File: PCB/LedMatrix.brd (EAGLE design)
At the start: 32.3 x 33.7 mm, 12 parts, among them IC1 74HC164D

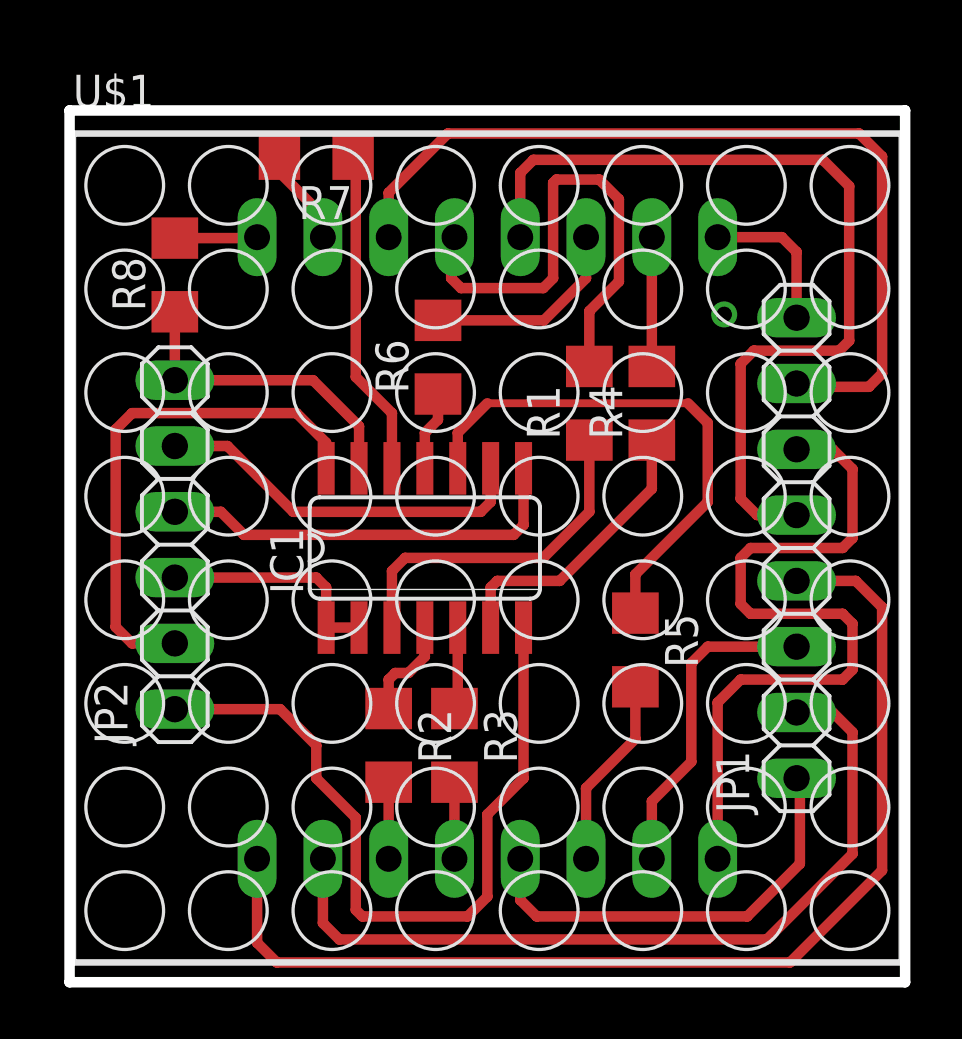
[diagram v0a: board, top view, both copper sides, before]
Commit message: Updated led matrix board.
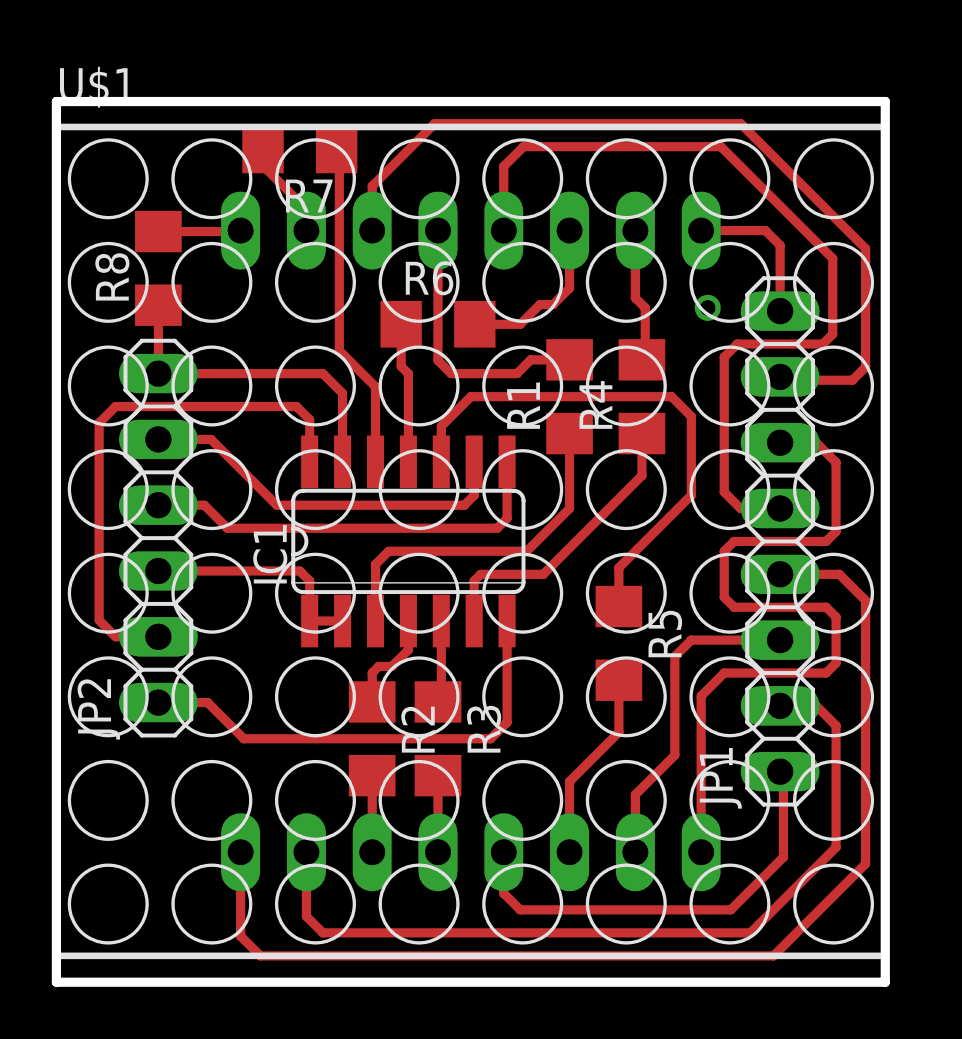
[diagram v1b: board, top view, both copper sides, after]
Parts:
- moved R6 1.27 mm to (14.7, 25.4), turned to 0 degrees
- moved R1 0.80 mm to (19.8, 22.6)
- moved U$1 0.68 mm to (16.0, 17.0)
- moved R3 0.68 mm to (14.7, 9.40)
- moved R5 0.68 mm to (21.7, 13.1)
- moved JP2 0.68 mm to (3.94, 17.1)
- moved R8 0.68 mm to (3.94, 27.6)
- moved IC1 0.68 mm to (13.6, 17.0)
- moved R7 0.68 mm to (9.40, 32.1)
- moved R2 0.68 mm to (12.2, 9.40)
- moved JP1 0.68 mm to (27.9, 17.0)
- moved R4 0.46 mm to (22.6, 22.6)
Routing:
- net GND: track 29.5 -> 18.2 mm
- net N$1: track 19.4 -> 10.5 mm
- net N$14: track 3.08 -> 5.42 mm
- net N$18: track 34.0 -> 31.9 mm
- net N$20: track 34.0 -> 32.4 mm
- net N$6: track 7.97 -> 6.46 mm
- net N$16: track 12.1 -> 12.7 mm
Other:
- board size 32.3 x 33.7 mm -> 32 x 34 mm

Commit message: Minor corrections to the led matrix board.
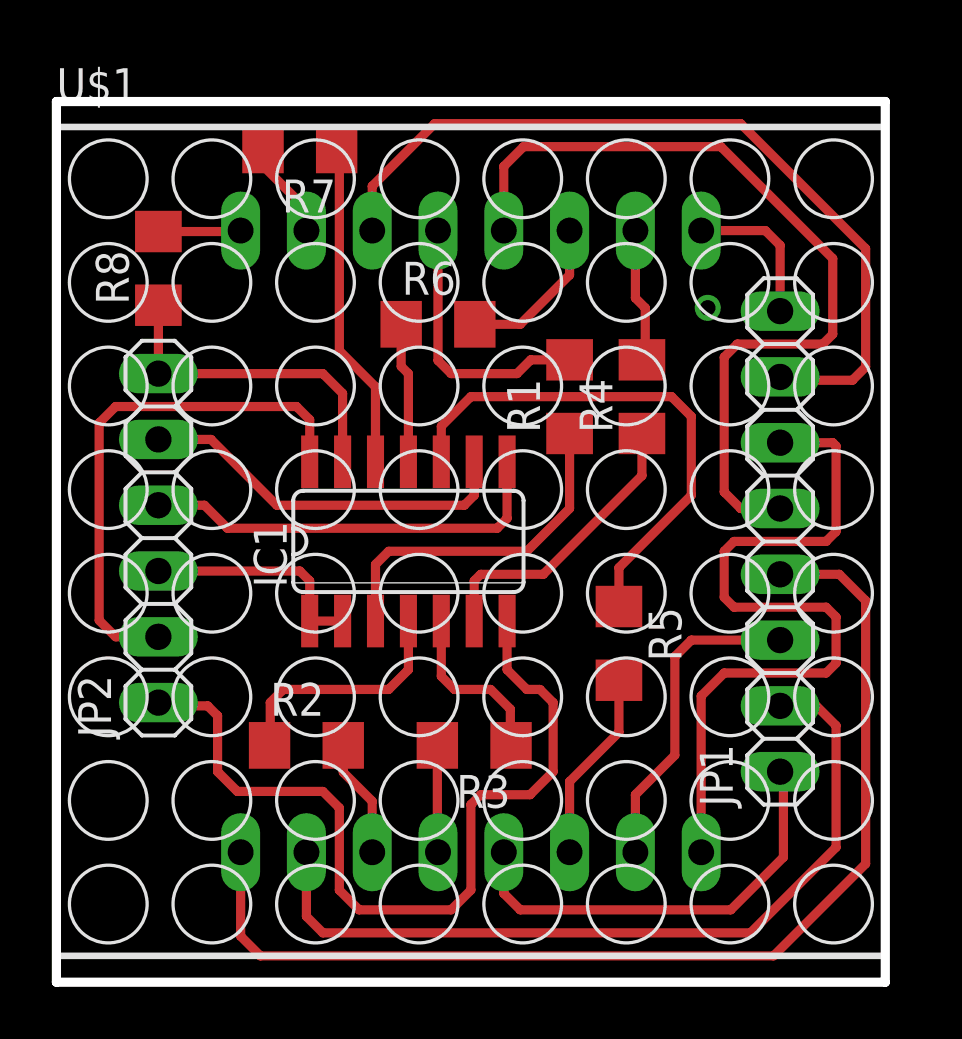
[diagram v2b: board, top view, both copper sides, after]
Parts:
- moved R2 2.55 mm to (9.65, 9.14), turned to 0 degrees
- moved R3 1.42 mm to (16.1, 9.14), turned to 180 degrees
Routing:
- net GND: track 18.2 -> 32.7 mm
- net N$10: track 4.00 -> 9.40 mm
- net N$11: track 3.18 -> 6.73 mm
- net N$2: track 2.96 -> 4.59 mm
- net N$3: track 2.96 -> 4.14 mm
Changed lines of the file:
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@@
 <setting verticaltext="up"/>
 </settings>
-<grid distance="1" unitdist="mm" unit="mm" style="lines" multiple="1" display="yes" altdistance="5" altunitdist="mil" altunit="mil"/>
+<grid distance="5" unitdist="mil" unit="mil" style="lines" multiple="1" display="yes" altdistance="5" altunitdist="mil" altunit="mil"/>
 <layers>
 <layer number="1" name="Top" color="4" fill="1" visible="yes" active="yes"/>
@@
 <element name="R1" library="resistor" package="R1206" value="200" x="19.812" y="22.606" rot="R90"/>
 <element name="U$1" library="led_matrix_8x8" package="NFM-12881BG-11" value="NFM-12881BG-11" x="16.002" y="17.018"/>
-<element name="R2" library="resistor" package="R1206" value="200" x="12.192" y="9.398" rot="R270"/>
-<element name="R3" library="resistor" package="R1206" value="200" x="14.732" y="9.398" rot="R270"/>
+<element name="R2" library="resistor" package="R1206" value="200" x="9.652" y="9.144"/>
+<element name="R3" library="resistor" package="R1206" value="200" x="16.129" y="9.144" rot="R180"/>
 <element name="R4" library="resistor" package="R1206" value="200" x="22.606" y="22.606" rot="R90"/>
 <element name="R5" library="resistor" package="R1206" value="200" x="21.717" y="13.081" rot="R270"/>
@@
 <contactref element="IC1" pad="7"/>
 <contactref element="JP2" pad="1"/>
-<wire x1="17.399" y1="13.9446" x2="17.399" y2="10.033" width="0.3556" layer="1"/>
-<wire x1="17.399" y1="10.033" x2="16.764" y2="9.398" width="0.3556" layer="1"/>
-<wire x1="16.764" y1="9.398" x2="7.239" y2="9.398" width="0.3556" layer="1"/>
-<wire x1="7.239" y1="9.398" x2="5.842" y2="10.795" width="0.3556" layer="1"/>
-<wire x1="5.842" y1="10.795" x2="3.937" y2="10.795" width="0.3556" layer="1"/>
+<wire x1="17.399" y1="13.9446" x2="17.399" y2="12.065" width="0.3556" layer="1"/>
+<wire x1="17.399" y1="12.065" x2="18.161" y2="11.303" width="0.3556" layer="1"/>
+<wire x1="18.161" y1="11.303" x2="18.669" y2="11.303" width="0.3556" layer="1"/>
+<wire x1="18.669" y1="11.303" x2="19.177" y2="10.795" width="0.3556" layer="1"/>
+<wire x1="19.177" y1="10.795" x2="19.177" y2="8.128" width="0.3556" layer="1"/>
+<wire x1="19.177" y1="8.128" x2="18.288" y2="7.239" width="0.3556" layer="1"/>
+<wire x1="18.288" y1="7.239" x2="16.383" y2="7.239" width="0.3556" layer="1"/>
+<wire x1="16.383" y1="7.239" x2="16.002" y2="6.858" width="0.3556" layer="1"/>
+<wire x1="16.002" y1="6.858" x2="16.002" y2="3.556" width="0.3556" layer="1"/>
+<wire x1="16.002" y1="3.556" x2="15.24" y2="2.794" width="0.3556" layer="1"/>
+<wire x1="15.24" y1="2.794" x2="11.684" y2="2.794" width="0.3556" layer="1"/>
+<wire x1="11.684" y1="2.794" x2="10.922" y2="3.556" width="0.3556" layer="1"/>
+<wire x1="10.922" y1="3.556" x2="10.922" y2="6.731" width="0.3556" layer="1"/>
+<wire x1="10.922" y1="6.731" x2="10.287" y2="7.366" width="0.3556" layer="1"/>
+<wire x1="10.287" y1="7.366" x2="6.985" y2="7.366" width="0.3556" layer="1"/>
+<wire x1="6.985" y1="7.366" x2="6.223" y2="8.128" width="0.3556" layer="1"/>
+<wire x1="6.223" y1="8.128" x2="6.223" y2="10.287" width="0.3556" layer="1"/>
+<wire x1="6.223" y1="10.287" x2="5.842" y2="10.668" width="0.3556" layer="1"/>
+<wire x1="5.842" y1="10.668" x2="4.064" y2="10.668" width="0.3556" layer="1"/>
+<wire x1="4.064" y1="10.668" x2="3.937" y2="10.795" width="0.3556" layer="1"/>
 </signal>
 <signal name="VCC">
@@
 <contactref element="U$1" pad="3"/>
 <contactref element="R2" pad="2"/>
-<wire x1="12.192" y1="7.976" x2="12.192" y2="5.018" width="0.3556" layer="1"/>
+<wire x1="11.074" y1="9.144" x2="11.074" y2="8.103" width="0.3556" layer="1"/>
+<wire x1="11.074" y1="8.103" x2="12.192" y2="6.985" width="0.3556" layer="1"/>
+<wire x1="12.192" y1="6.985" x2="12.192" y2="5.018" width="0.3556" layer="1"/>
 </signal>
 <signal name="N$3">
 <contactref element="U$1" pad="4"/>
 <contactref element="R3" pad="2"/>
-<wire x1="14.732" y1="7.976" x2="14.732" y2="5.018" width="0.3556" layer="1"/>
+<wire x1="14.707" y1="9.144" x2="14.707" y2="5.043" width="0.3556" layer="1"/>
+<wire x1="14.707" y1="5.043" x2="14.732" y2="5.018" width="0.3556" layer="1"/>
 </signal>
 <signal name="N$4">
@@
 <contactref element="U$1" pad="11"/>
 <contactref element="R6" pad="2"/>
-<wire x1="19.812" y1="29.018" x2="19.812" y2="26.797" width="0.3556" layer="1"/>
-<wire x1="19.812" y1="26.797" x2="19.177" y2="26.162" width="0.3556" layer="1"/>
-<wire x1="19.177" y1="26.162" x2="18.669" y2="26.162" width="0.3556" layer="1"/>
-<wire x1="18.669" y1="26.162" x2="17.907" y2="25.4" width="0.3556" layer="1"/>
+<wire x1="19.812" y1="29.018" x2="19.812" y2="27.305" width="0.3556" layer="1"/>
+<wire x1="19.812" y1="27.305" x2="17.907" y2="25.4" width="0.3556" layer="1"/>
 <wire x1="17.907" y1="25.4" x2="16.154" y2="25.4" width="0.3556" layer="1"/>
 </signal>
@@
 <contactref element="R2" pad="1"/>
 <contactref element="IC1" pad="4"/>
-<wire x1="13.589" y1="13.9446" x2="13.589" y2="12.827" width="0.3556" layer="1"/>
-<wire x1="13.589" y1="12.827" x2="12.954" y2="12.192" width="0.3556" layer="1"/>
-<wire x1="12.954" y1="12.192" x2="12.446" y2="12.192" width="0.3556" layer="1"/>
-<wire x1="12.446" y1="12.192" x2="12.192" y2="11.938" width="0.3556" layer="1"/>
-<wire x1="12.192" y1="11.938" x2="12.192" y2="10.82" width="0.3556" layer="1"/>
+<wire x1="13.589" y1="13.9446" x2="13.589" y2="12.065" width="0.3556" layer="1"/>
+<wire x1="13.589" y1="12.065" x2="12.827" y2="11.303" width="0.3556" layer="1"/>
+<wire x1="12.827" y1="11.303" x2="8.763" y2="11.303" width="0.3556" layer="1"/>
+<wire x1="8.763" y1="11.303" x2="8.255" y2="10.795" width="0.3556" layer="1"/>
+<wire x1="8.255" y1="10.795" x2="8.255" y2="9.169" width="0.3556" layer="1"/>
+<wire x1="8.255" y1="9.169" x2="8.23" y2="9.144" width="0.3556" layer="1"/>
 </signal>
 <signal name="N$11">
 <contactref element="R3" pad="1"/>
 <contactref element="IC1" pad="5"/>
-<wire x1="14.859" y1="13.9446" x2="14.859" y2="10.947" width="0.3556" layer="1"/>
-<wire x1="14.859" y1="10.947" x2="14.732" y2="10.82" width="0.3556" layer="1"/>
+<wire x1="14.859" y1="13.9446" x2="14.859" y2="11.811" width="0.3556" layer="1"/>
+<wire x1="14.859" y1="11.811" x2="15.367" y2="11.303" width="0.3556" layer="1"/>
+<wire x1="15.367" y1="11.303" x2="16.764" y2="11.303" width="0.3556" layer="1"/>
+<wire x1="16.764" y1="11.303" x2="17.526" y2="10.541" width="0.3556" layer="1"/>
+<wire x1="17.526" y1="10.541" x2="17.526" y2="9.169" width="0.3556" layer="1"/>
+<wire x1="17.526" y1="9.169" x2="17.551" y2="9.144" width="0.3556" layer="1"/>
 </signal>
 <signal name="N$12">
@@
 <wire x1="26.162" y1="17.018" x2="29.718" y2="17.018" width="0.3556" layer="1"/>
 <wire x1="29.718" y1="17.018" x2="30.099" y2="17.399" width="0.3556" layer="1"/>
-<wire x1="30.099" y1="17.399" x2="30.099" y2="20.066" width="0.3556" layer="1"/>
-<wire x1="30.099" y1="20.066" x2="29.337" y2="20.828" width="0.3556" layer="1"/>
-<wire x1="29.337" y1="20.828" x2="27.94" y2="20.828" width="0.3556" layer="1"/>
+<wire x1="30.099" y1="17.399" x2="30.099" y2="20.701" width="0.3556" layer="1"/>
+<wire x1="29.972" y1="20.828" x2="27.94" y2="20.828" width="0.3556" layer="1"/>
+<wire x1="29.972" y1="20.828" x2="30.099" y2="20.701" width="0.3556" layer="1"/>
 </signal>
 <signal name="N$20">
@@
 <wire x1="17.399" y1="17.907" x2="17.018" y2="17.526" width="0.3556" layer="1"/>
 <contactref element="JP2" pad="4"/>
-<wire x1="6.604" y1="17.526" x2="5.715" y2="18.415" width="0.3556" layer="1"/>
 <wire x1="5.715" y1="18.415" x2="3.937" y2="18.415" width="0.3556" layer="1"/>
+<wire x1="5.715" y1="18.415" x2="6.604" y2="17.526" width="0.3556" layer="1"/>
 </signal>
 <signal name="N$25">

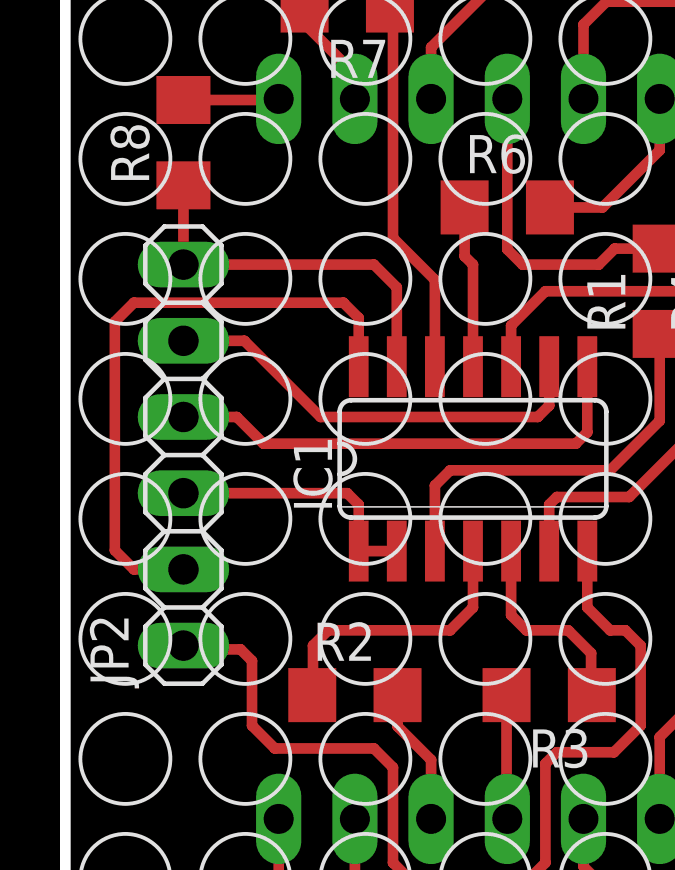
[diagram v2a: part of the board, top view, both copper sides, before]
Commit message: Minor measure corrections on the matrix board.
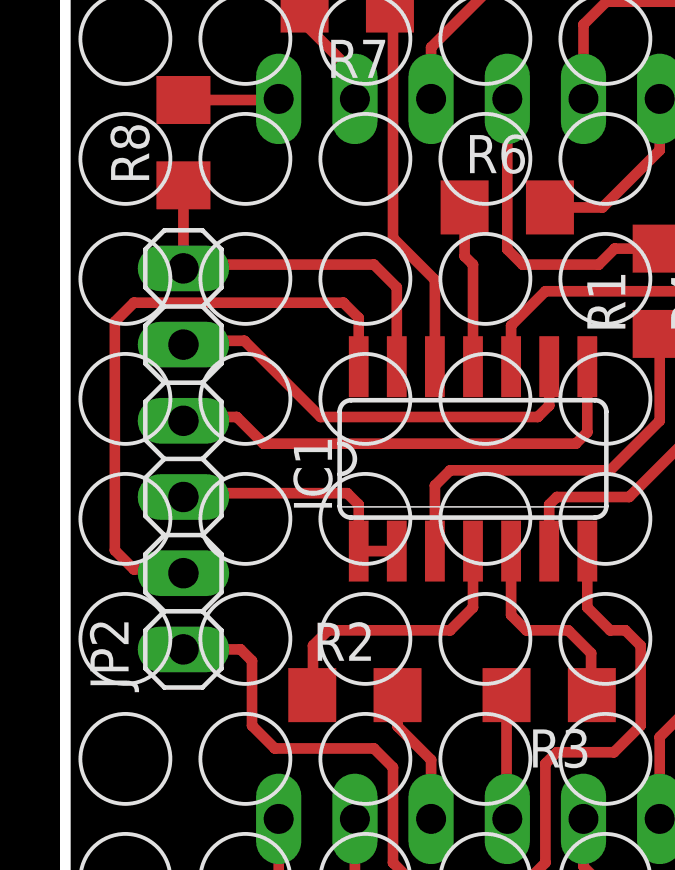
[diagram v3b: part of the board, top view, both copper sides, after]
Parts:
- moved JP2 0.13 mm to (3.94, 17.0)
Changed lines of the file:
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@@
 <dimension x1="0" y1="0" x2="4" y2="0" x3="2" y3="-3" textsize="1.016" layer="47"/>
 <dimension x1="32" y1="0" x2="28" y2="0" x3="30" y3="-3" textsize="1.016" layer="47"/>
+<dimension x1="0" y1="0" x2="0" y2="17" x3="37" y3="8.5" textsize="1.016" layer="47"/>
 </plain>
 <attributes>
@@
 <element name="R8" library="resistor" package="R1206" value="200" x="3.937" y="27.559" rot="R90"/>
 <element name="JP1" library="pinhead" package="1X08" value="" x="27.94" y="17.018" rot="R90"/>
-<element name="JP2" library="pinhead" package="1X06" value="" x="3.937" y="17.145" rot="R90"/>
+<element name="JP2" library="pinhead" package="1X06" value="" x="3.937" y="17.018" rot="R90"/>
 </elements>
 <signals>
@@
 <wire x1="6.223" y1="8.128" x2="6.223" y2="10.287" width="0.3556" layer="1"/>
 <wire x1="6.223" y1="10.287" x2="5.842" y2="10.668" width="0.3556" layer="1"/>
-<wire x1="5.842" y1="10.668" x2="4.064" y2="10.668" width="0.3556" layer="1"/>
-<wire x1="4.064" y1="10.668" x2="3.937" y2="10.795" width="0.3556" layer="1"/>
+<wire x1="3.937" y1="10.668" x2="5.842" y2="10.668" width="0.3556" layer="1"/>
 </signal>
 <signal name="VCC">
@@
 <contactref element="JP2" pad="2"/>
 <wire x1="9.271" y1="22.225" x2="2.286" y2="22.225" width="0.3556" layer="1"/>
-<wire x1="3.937" y1="13.335" x2="2.286" y2="13.335" width="0.3556" layer="1"/>
 <wire x1="2.286" y1="13.335" x2="1.651" y2="13.97" width="0.3556" layer="1"/>
 <wire x1="1.651" y1="13.97" x2="1.651" y2="21.59" width="0.3556" layer="1"/>
@@
 <wire x1="9.779" y1="20.0914" x2="9.779" y2="21.717" width="0.3556" layer="1"/>
 <wire x1="9.779" y1="21.717" x2="9.271" y2="22.225" width="0.3556" layer="1"/>
+<wire x1="2.286" y1="13.335" x2="3.81" y2="13.335" width="0.3556" layer="1"/>
+<wire x1="3.81" y1="13.335" x2="3.937" y2="13.208" width="0.3556" layer="1"/>
 </signal>
 <signal name="N$1">
@@
 <contactref element="IC1" pad="13"/>
 <contactref element="JP2" pad="6"/>
-<wire x1="10.287" y1="23.495" x2="3.937" y2="23.495" width="0.3556" layer="1"/>
-<wire x1="3.937" y1="23.495" x2="3.937" y2="26.137" width="0.3556" layer="1"/>
 <wire x1="11.049" y1="20.0914" x2="11.049" y2="22.733" width="0.3556" layer="1"/>
 <wire x1="11.049" y1="22.733" x2="10.287" y2="23.495" width="0.3556" layer="1"/>
+<wire x1="10.287" y1="23.495" x2="4.064" y2="23.495" width="0.3556" layer="1"/>
+<wire x1="4.064" y1="23.495" x2="3.937" y2="23.368" width="0.3556" layer="1"/>
+<wire x1="3.937" y1="26.137" x2="3.937" y2="23.368" width="0.3556" layer="1"/>
 </signal>
 <signal name="N$17">
@@
 <wire x1="11.049" y1="13.9446" x2="9.779" y2="13.9446" width="0.3556" layer="1"/>
 <contactref element="JP2" pad="3"/>
-<wire x1="3.937" y1="15.875" x2="9.398" y2="15.875" width="0.3556" layer="1"/>
 <wire x1="9.398" y1="15.875" x2="9.779" y2="15.494" width="0.3556" layer="1"/>
 <wire x1="9.779" y1="15.494" x2="9.779" y2="13.9446" width="0.3556" layer="1"/>
+<wire x1="9.398" y1="15.875" x2="4.064" y2="15.875" width="0.3556" layer="1"/>
+<wire x1="4.064" y1="15.875" x2="3.937" y2="15.748" width="0.3556" layer="1"/>
 </signal>
 <signal name="N$27">
@@
 <wire x1="17.399" y1="17.907" x2="17.018" y2="17.526" width="0.3556" layer="1"/>
 <contactref element="JP2" pad="4"/>
-<wire x1="5.715" y1="18.415" x2="3.937" y2="18.415" width="0.3556" layer="1"/>
 <wire x1="5.715" y1="18.415" x2="6.604" y2="17.526" width="0.3556" layer="1"/>
+<wire x1="5.715" y1="18.415" x2="4.064" y2="18.415" width="0.3556" layer="1"/>
+<wire x1="4.064" y1="18.415" x2="3.937" y2="18.288" width="0.3556" layer="1"/>
 </signal>
 <signal name="N$25">
@@
 <wire x1="15.748" y1="18.415" x2="8.509" y2="18.415" width="0.3556" layer="1"/>
 <wire x1="8.509" y1="18.415" x2="5.969" y2="20.955" width="0.3556" layer="1"/>
-<wire x1="5.969" y1="20.955" x2="3.937" y2="20.955" width="0.3556" layer="1"/>
+<wire x1="5.969" y1="20.955" x2="4.064" y2="20.955" width="0.3556" layer="1"/>
+<wire x1="4.064" y1="20.955" x2="3.937" y2="20.828" width="0.3556" layer="1"/>
 </signal>
 </signals>
